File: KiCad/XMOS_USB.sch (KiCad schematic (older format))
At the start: 31 parts, among them J5 USB_B_Mini, U10 TPD2E2U06, U9 XUF216-512-FB236, X1 ASV-24MHz

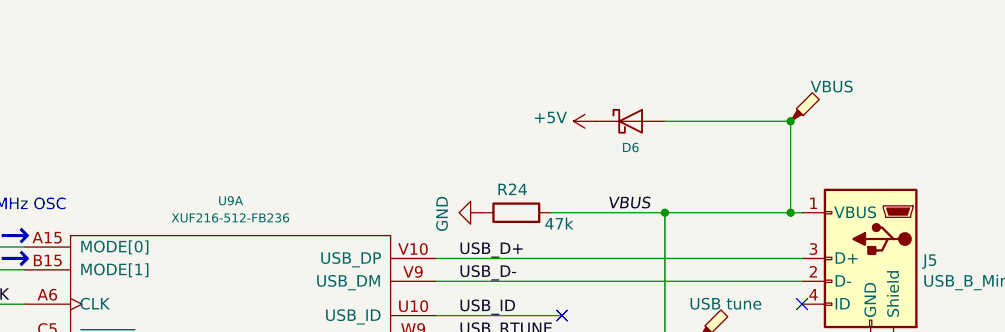
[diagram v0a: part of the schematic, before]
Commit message: Added impedance calc, and rerouted USB
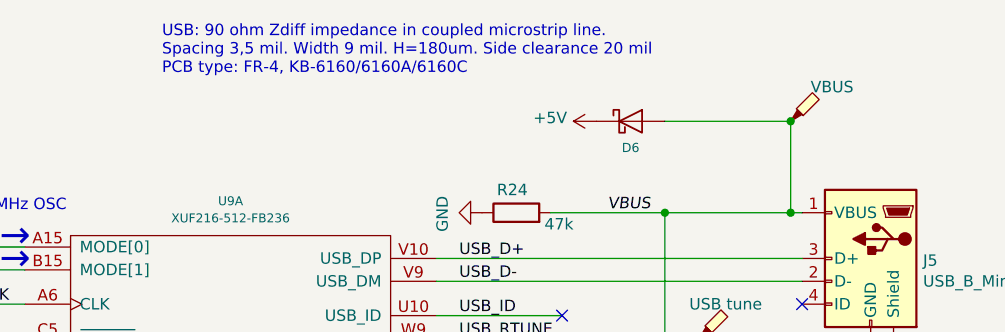
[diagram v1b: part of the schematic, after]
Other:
- note added: "USB: 90 ohm Zdiff impedance in coupled microstrip line.\nSpacing 3,5 mil. Width 9 mil. H=180um. Side clearance 20 mil\nPCB type: FR-4, KB-6160/6160A/6160C"
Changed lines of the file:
@@
 	1    0    0    -1
 $EndComp
+Text Notes 5950 1000 0    50   ~ 0
+USB: 90 ohm Zdiff impedance in coupled microstrip line.\nSpacing 3,5 mil. Width 9 mil. H=180um. Side clearance 20 mil\nPCB type: FR-4, KB-6160/6160A/6160C
 $EndSCHEMATC

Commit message: Many small fixes
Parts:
- C20: footprint Capacitor_SMD:C_0402_1005Metric -> Capacitor_SMD:C_0603_1608Metric_Pad1.05x0.95mm_HandSolder
- C33, C40: footprint Capacitor_SMD:C_0402_1005Metric -> Capacitor_SMD:C_0603_1608Metric
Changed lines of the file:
@@
 F 0 "C33" H 4615 3396 50  0000 L CNN
 F 1 "100nF" H 4600 3250 50  0000 L CNN
-F 2 "Capacitor_SMD:C_0402_1005Metric" H 4538 3200 50  0001 C CNN
+F 2 "Capacitor_SMD:C_0603_1608Metric" H 4538 3200 50  0001 C CNN
 F 3 "~" H 4500 3350 50  0001 C CNN
 F 4 "~" H 0   0   50  0001 C CNN "Part Number"
@@
 F 0 "C40" H 7350 2600 50  0000 L CNN
 F 1 "100nF" H 7350 2500 50  0000 L CNN
-F 2 "Capacitor_SMD:C_0402_1005Metric" H 7638 2450 50  0001 C CNN
+F 2 "Capacitor_SMD:C_0603_1608Metric" H 7638 2450 50  0001 C CNN
 F 3 "~" H 7600 2600 50  0001 C CNN
 F 4 "~" H 0   0   50  0001 C CNN "Part Number"
@@
 F 0 "C20" H 2000 2100 50  0000 L CNN
 F 1 "10-100nF" H 1800 1900 50  0000 L CNN
-F 2 "Capacitor_SMD:C_0402_1005Metric" H 2288 1850 50  0001 C CNN
+F 2 "Capacitor_SMD:C_0603_1608Metric_Pad1.05x0.95mm_HandSolder" H 2288 1850 50  0001 C CNN
 F 3 "~" H 2250 2000 50  0001 C CNN
 F 4 "~" H 0   0   50  0001 C CNN "Part Number"
